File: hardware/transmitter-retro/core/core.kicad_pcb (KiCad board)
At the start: 2 copper layers, 100 x 90 mm, 64 parts, among them J1 Input, J2 Output, J3 Power, J4 Expansion, U1 556, U10 74LS163, U11 TLC7524CN, U12 74LS245, U13 74LS153, U14 74LS04, U15 74LS74, U16 74LS74, U18 74LS32, U19 74LS08, U2 74LS163, U21 LM339, U6 74LS153, U7 74LS273, U8 74LS165, U9 74LS163, Y1 4Mz

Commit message: Update part numbers Swap out input connector footprint Placement tweaks
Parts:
- removed C19: .01uF, Capacitor_THT:C_Rect_L4.6mm_W2.0mm_P2.50mm_MKS02_FKP02
- removed C29, C30: CP1, Capacitor_THT:CP_Radial_D4.0mm_P1.50mm
- removed C35: .001uF, Capacitor_THT:C_Rect_L4.6mm_W2.0mm_P2.50mm_MKS02_FKP02
- removed U18: 74LS32, Package_DIP:DIP-14_W7.62mm
- removed U19: 74LS08, Package_DIP:DIP-14_W7.62mm
- removed U21: LM339, Package_DIP:DIP-14_W7.62mm
- removed Y1: 4Mz, Crystal:Crystal_HC49-U_Vertical
- added C22: CP1, Capacitor_THT:CP_Radial_D4.0mm_P1.50mm, F.Cu at (170.4, 61.3)
- added R12: 10k, Resistor_THT:R_Axial_DIN0207_L6.3mm_D2.5mm_P10.16mm_Horizontal, F.Cu at (166.1, 136.5)
- added R13: 10k, Resistor_THT:R_Axial_DIN0207_L6.3mm_D2.5mm_P10.16mm_Horizontal, F.Cu at (143.4, 136.5)
- added R14: 10k, Resistor_THT:R_Axial_DIN0207_L6.3mm_D2.5mm_P10.16mm_Horizontal, F.Cu at (129.3, 92.6)
- added R15: 10k, Resistor_THT:R_Axial_DIN0207_L6.3mm_D2.5mm_P10.16mm_Horizontal, F.Cu at (177.5, 114.0)
- added R3: 1M, Resistor_THT:R_Axial_DIN0207_L6.3mm_D2.5mm_P10.16mm_Horizontal, F.Cu at (102.9, 52.3)
- added U17: ULN2003A, Package_DIP:DIP-16_W7.62mm, F.Cu at (103.9, 120.4)
- added U3: 74LS163, Package_DIP:DIP-16_W7.62mm, F.Cu at (133.6, 59.7)
- added U4: 74LS74, Package_DIP:DIP-14_W7.62mm, F.Cu at (144.7, 70.6)
- added U5: 74LS74, Package_DIP:DIP-14_W7.62mm, F.Cu at (156.1, 70.4)
- C21: value .01uF -> CP1; footprint Capacitor_THT:C_Rect_L4.6mm_W2.0mm_P2.50mm_MKS02_FKP02 -> Capacitor_THT:CP_Radial_D4.0mm_P1.50mm
- J1: footprint Connector_PinHeader_2.54mm:PinHeader_2x08_P2.54mm_Vertical -> Connector_IDC:IDC-Header_2x08_P2.54mm_Horizontal
- R10, R9: value 100k -> 10k
- R6, R7: value 2.2k -> 10k
- U10: value 74LS163 -> 74LS165
- U11: value TLC7524CN -> 74LS151
- U12: value 74LS245 -> 74LS163; footprint Package_DIP:DIP-20_W7.62mm -> Package_DIP:DIP-16_W7.62mm
- U13: value 74LS153 -> 74LS163
- U14: value 74LS04 -> 74LS373; footprint Package_DIP:DIP-14_W7.62mm -> Package_DIP:DIP-20_W7.62mm
- U15: value 74LS74 -> TLC7524CN; footprint Package_DIP:DIP-14_W7.62mm -> Package_DIP:DIP-20_W7.62mm
- U16: value 74LS74 -> LM339; footprint Package_DIP:DIP-14_W7.62mm -> Package_DIP:DIP-16_W7.62mm
- U2: value 74LS163 -> 74LS151
- U6: value 74LS153 -> 74LS08; footprint Package_DIP:DIP-16_W7.62mm -> Package_DIP:DIP-14_W7.62mm
- U7: value 74LS273 -> 74LS32; footprint Package_DIP:DIP-20_W7.62mm -> Package_DIP:DIP-14_W7.62mm
- U8: value 74LS165 -> 74LS04; footprint Package_DIP:DIP-16_W7.62mm -> Package_DIP:DIP-14_W7.62mm
- U9: value 74LS163 -> 74LS02; footprint Package_DIP:DIP-16_W7.62mm -> Package_DIP:DIP-14_W7.62mm
- moved R9 86.4 mm to (144.7, 53.2), turned to 270 degrees
- moved C5 83.6 mm to (166.6, 70.1)
- moved R8 83.3 mm to (152.0, 53.2), turned to 270 degrees
- moved R10 76.4 mm to (167.5, 75.9), turned to 270 degrees
- moved U9 68.8 mm to (156.1, 117.6)
- moved C21 68.8 mm to (170.4, 56.0), turned to 0 degrees
- moved C9 68.7 mm to (163.4, 114.4)
- moved J3 67.6 mm to (164.0, 59.9), turned to 180 degrees
- moved U10 66.4 mm to (166.5, 115.1)
- moved C10 66.2 mm to (173.9, 111.9)
- moved U12 63.9 mm to (145.8, 115.2)
- moved C12 63.5 mm to (153.2, 111.8)
- moved D1 60.2 mm to (156.2, 64.9), turned to 0 degrees
- moved C33 59.7 mm to (117.9, 62.0)
- moved R7 58.3 mm to (148.3, 53.2), turned to 270 degrees
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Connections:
- A1 pad 1: /SAMPLE_LATCH -> /~SAMPLE_OVERRIDE
- A1 pad 10: /SHIFT_TRANSMIT -> /~SHIFT_ENABLE
- A1 pad 11: /CLK_RX -> /SHIFT_TRANSMIT
- A1 pad 12: /monitor/DATA_RX_IN -> /DATA_RX
- A1 pad 13: /CLK_FAST -> /CLK_RX
- A1 pad 14: /CLK_SLOW -> /CLK_FAST
- A1 pad 15: /~SAMPLE_ASSERT -> /CLK_SLOW
- A1 pad 5: /~SAMPLE_RESET -> /SAMPLE_LATCH
- A1 pad 6: /SAMPLE_SEL0 -> /~SAMPLE_RESET
- A1 pad 7: /SAMPLE_SEL1 -> /SAMPLE_SEL0
- A1 pad 8: /~SHIFT_LOAD -> /SAMPLE_SEL1
- A1 pad 9: /SHIFT_DISABLE -> /~SHIFT_LOAD
- J1 pad 3: /monitor/DATA_RX_IN -> /shift/~CLK_OUT
- J1 pad 5: /CLK_RX -> /shift/~DATA_OUT
- J2 pad 3: /monitor/DATA_RX_IN -> /DATA_RX
- J4 pad 10: /~SAMPLE_RESET -> /SAMPLE_LATCH
- J4 pad 12: /SAMPLE_SEL0 -> /~SAMPLE_RESET
- J4 pad 14: /SAMPLE_SEL1 -> /SAMPLE_SEL0
- J4 pad 16: /~SHIFT_LOAD -> /SAMPLE_SEL1
- J4 pad 18: /SHIFT_DISABLE -> /~SHIFT_LOAD
- J4 pad 20: /SHIFT_TRANSMIT -> /~SHIFT_ENABLE
- J4 pad 21: /CLK_TX -> /~BUS_ACK
- J4 pad 22: /DATA_FIXED -> /SHIFT_TRANSMIT
- J4 pad 23: /CLK_RX -> /~BUS_REQ
- J4 pad 24: /~FRAME_RESET -> Net-(J4-Pad24)
- J4 pad 25: /CLK_FAST -> /SAMPLE_REF
- J4 pad 26: Net-(J4-Pad26) -> /~FRAME_RESET
- J4 pad 27: /CLK_SLOW -> /CLK_EXT
- J4 pad 28: Net-(J4-Pad28) -> /DATA_RX
- J4 pad 29: Net-(J4-Pad29) -> /CLK_TX
- J4 pad 30: Net-(J4-Pad30) -> /DATA_FIXED
- J4 pad 31: Net-(J4-Pad31) -> /CLK_RX
- J4 pad 32: Net-(J4-Pad32) -> /DATA_SHIFT
- J4 pad 33: Net-(J4-Pad33) -> /CLK_FAST
- J4 pad 34: Net-(J4-Pad34) -> GND
- J4 pad 35: Net-(J4-Pad35) -> /CLK_SLOW
- J4 pad 36: Net-(J4-Pad36) -> GND
- J4 pad 37: GND -> Net-(J4-Pad37)
- J4 pad 39: GND -> /~CLK_EXT_SEL
- J4 pad 6: /~SAMPLE_ASSERT -> /SAMPLE_COUNT
- J4 pad 8: /SAMPLE_LATCH -> /~SAMPLE_OVERRIDE
- R10 pad 1: /clock/~CLK_SLOW_IN -> +5V
- R10 pad 2: GND -> /shift/~CLK_STEP_IN
- R11 pad 2: /shift/~CLK_STEP_IN -> /clock/~CLK_STEP_INA
- R6 pad 1: Net-(R6-Pad1) -> +5V
- R6 pad 2: Net-(R6-Pad2) -> /CLK_EXT
- R7 pad 1: Net-(R7-Pad1) -> +5V
- R7 pad 2: Net-(R6-Pad1) -> /clock/~CLK_SLOW_IN
- R8 pad 1: /clock/~CLK_STEP_INA -> +5V
- R8 pad 2: GND -> /clock/~CLK_FAST_IN
- R9 pad 1: /clock/~CLK_FAST_IN -> +5V
- R9 pad 2: GND -> /~CLK_EXT_SEL
- U1 pad 5: Net-(U1-Pad5) -> /clock/CLK_SLOW
- U1 pad 9: Net-(U1-Pad9) -> /clock/CLK_FAST
- U10 pad 1: /~SAMPLE_RESET -> /~SHIFT_LOAD
- U10 pad 10: Net-(U10-Pad10) -> GND
- U10 pad 11: /sample/DO7 -> /shift/D0
- U10 pad 12: /sample/DO6 -> /shift/D1
- U10 pad 13: /sample/DO5 -> /shift/D2
- U10 pad 14: /sample/DO4 -> /shift/D3
- U10 pad 15: Net-(U10-Pad15) -> /~SHIFT_ENABLE
- U10 pad 2: /clock/CLK_SAMPLE_OUT -> /CLK_TX
- U10 pad 3: GND -> /shift/D4
- U10 pad 4: GND -> /shift/D5
- U10 pad 5: GND -> /shift/D6
- U10 pad 6: GND -> /shift/D7
- U10 pad 7: +5V -> Net-(U10-Pad7)
- U10 pad 9: +5V -> /DATA_SHIFT
- U11 pad 1: +5V -> Net-(U11-Pad1)
- U11 pad 10: /sample/DO1 -> Net-(U11-Pad10)
- U11 pad 11: /sample/DO0 -> Net-(U11-Pad11)
- U11 pad 12: GND -> Net-(U11-Pad12)
- U11 pad 13: /clock/CLK_SAMPLE_OUT -> Net-(U11-Pad13)
- U11 pad 14: +5V -> Net-(U11-Pad14)
- U11 pad 15: Net-(U11-Pad15) -> /SAMPLE_COUNT
- U11 pad 16: Net-(U11-Pad16) -> +5V
- U11 pad 2: GND -> Net-(U11-Pad2)
- U11 pad 3: GND -> Net-(U11-Pad3)
- U11 pad 4: /sample/DO7 -> Net-(U11-Pad4)
- U11 pad 5: /sample/DO6 -> Net-(U11-Pad5)
- U11 pad 6: /sample/DO5 -> Net-(U11-Pad6)
- U11 pad 7: /sample/DO4 -> GND
- U11 pad 8: /sample/DO3 -> GND
- U11 pad 9: /sample/DO2 -> /~SAMPLE_OVERRIDE
- U12 pad 1: +5V -> /~SAMPLE_RESET
- U12 pad 10: GND -> Net-(U12-Pad10)
- U12 pad 11: /sample/D7 -> /sample/DO3
- U12 pad 12: /sample/D6 -> /sample/DO2
- U12 pad 13: /sample/D5 -> /sample/D01
- U12 pad 14: /sample/D4 -> /sample/DO0
- U12 pad 15: /sample/D3 -> Net-(U12-Pad15)
- U12 pad 16: /sample/D2 -> +5V
- U12 pad 2: Net-(U12-Pad2) -> /clock/CLK_SAMPLE_OUT
- U12 pad 3: Net-(U12-Pad3) -> GND
- U12 pad 4: Net-(U12-Pad4) -> GND
- U12 pad 5: Net-(U12-Pad5) -> GND
- U12 pad 6: Net-(U12-Pad6) -> GND
- U12 pad 7: Net-(U12-Pad7) -> Net-(U11-Pad5)
- U12 pad 8: Net-(U12-Pad8) -> GND
- U12 pad 9: Net-(U12-Pad9) -> +5V
- U13 pad 1: GND -> /~SAMPLE_RESET
- U13 pad 10: GND -> Net-(U12-Pad15)
- U13 pad 11: GND -> /sample/DO7
- U13 pad 12: GND -> /sample/DO6
- U13 pad 13: GND -> /sample/DO5
- U13 pad 14: /CLK_SLOW -> /sample/DO4
- U13 pad 15: GND -> Net-(U13-Pad15)
- U13 pad 2: /CLK_FAST -> /clock/CLK_SAMPLE_OUT
- U13 pad 3: Net-(U13-Pad3) -> GND
- U13 pad 4: Net-(U1-Pad5) -> GND
- U13 pad 5: Net-(U1-Pad9) -> GND
- U13 pad 6: Net-(R7-Pad1) -> GND
- U13 pad 7: /clock/CLK_SAMPLE_OUT -> +5V
- U13 pad 9: Net-(U13-Pad9) -> +5V
- U14 pad 1: Net-(R6-Pad2) -> Net-(U14-Pad1)
- U14 pad 10: Net-(U14-Pad10) -> GND
- U14 pad 11: Net-(U10-Pad15) -> /SAMPLE_LATCH
- U14 pad 12: Net-(U14-Pad12) -> /sample/D4
- U14 pad 13: Net-(U14-Pad13) -> /sample/DO4
- U14 pad 14: +5V -> /sample/DO5
- U14 pad 2: Net-(R6-Pad1) -> /sample/D0
- U14 pad 3: Net-(R6-Pad1) -> /sample/DO0
- U14 pad 4: Net-(R7-Pad1) -> /sample/D01
- U14 pad 5: Net-(U14-Pad5) -> /sample/D1
- U14 pad 6: Net-(U14-Pad6) -> /sample/D2
- U14 pad 7: GND -> /sample/DO2
- U14 pad 8: /CLK_RX -> /sample/DO3
- U14 pad 9: /CLK_TX -> /sample/D3
- U15 pad 10: Net-(U14-Pad12) -> /sample/DO1
- U15 pad 11: Net-(U13-Pad3) -> /sample/DO0
- U15 pad 12: /CLK_TX -> GND
- U15 pad 13: Net-(U15-Pad13) -> /clock/CLK_SAMPLE_OUT
- U15 pad 2: Net-(U15-Pad2) -> GND
- U15 pad 3: Net-(U1-Pad9) -> GND
- U15 pad 4: +5V -> /sample/DO7
- U15 pad 5: Net-(U15-Pad5) -> /sample/DO6
- U15 pad 6: Net-(U15-Pad6) -> /sample/DO5
- U15 pad 7: GND -> /sample/DO4
- U15 pad 8: Net-(U15-Pad8) -> /sample/DO3
- U15 pad 9: Net-(U15-Pad9) -> /sample/DO2
- U16 pad 1: Net-(U16-Pad1) -> Net-(U11-Pad3)
- U16 pad 10: Net-(U16-Pad10) -> /SAMPLE_REF
- U16 pad 11: /CLK_TX -> /sample/DIM_2_IN
- U16 pad 12: /clock/~CLK_FAST_IN -> GND
- U16 pad 13: Net-(U16-Pad10) -> Net-(U11-Pad2)
- U16 pad 14: +5V -> Net-(U11-Pad1)
- U16 pad 2: /clock/~CLK_SLOW_IN -> Net-(U11-Pad4)
- U16 pad 3: /CLK_TX -> +5V
- U16 pad 4: Net-(U16-Pad1) -> /SAMPLE_REF
- U16 pad 5: /CLK_SLOW -> /sample/DIM_4_IN
- U16 pad 6: Net-(U16-Pad6) -> /SAMPLE_REF
- U16 pad 7: GND -> /sample/DIM_3_IN
- U16 pad 8: Net-(U16-Pad8) -> /SAMPLE_REF
- U16 pad 9: /CLK_FAST -> /sample/DIM_1_IN
- U2 pad 1: +5V -> /clock/CLK_STEP
- U2 pad 10: +5V -> /CLK_FAST
- U2 pad 11: /CLK_TX -> /CLK_SLOW
- U2 pad 2: /clock/CLK_SAMPLE_OUT -> /clock/CLK_SLOW
- U2 pad 3: GND -> /clock/CLK_FAST
- U2 pad 4: GND -> /CLK_EXT
- U2 pad 5: GND -> /clock/CLK_SAMPLE_OUT
- U2 pad 6: GND -> Net-(U2-Pad6)
- U2 pad 7: +5V -> GND
- U2 pad 9: +5V -> GND
- U6 pad 1: GND -> /DATA_SHIFT
- U6 pad 10: GND -> Net-(U6-Pad10)
- U6 pad 11: GND -> Net-(U5-Pad2)
- U6 pad 12: GND -> /shift/~CLK_STEP_IN
- U6 pad 13: GND -> /clock/~CLK_STEP_INA
- U6 pad 14: /SAMPLE_SEL0 -> +5V
- U6 pad 2: /SAMPLE_SEL1 -> /SHIFT_TRANSMIT
- U6 pad 3: Net-(U21-Pad14) -> Net-(U6-Pad3)
- U6 pad 4: Net-(U21-Pad13) -> /clock/CLK_FAST
- U6 pad 5: Net-(U21-Pad1) -> Net-(U6-Pad5)
- U6 pad 6: Net-(U21-Pad2) -> /clock/CLK_STEP
- U6 pad 7: Net-(U6-Pad7) -> GND
- U6 pad 8: GND -> Net-(U6-Pad8)
- U6 pad 9: Net-(U6-Pad9) -> Net-(U5-Pad13)
- U7 pad 1: +5V -> Net-(U6-Pad3)
- U7 pad 10: GND -> Net-(U5-Pad2)
- U7 pad 11: /SAMPLE_LATCH -> Net-(U6-Pad5)
- U7 pad 12: Net-(U12-Pad6) -> /CLK_TX
- U7 pad 13: /sample/DO4 -> Net-(U5-Pad8)
- U7 pad 14: /sample/DO5 -> +5V
- U7 pad 2: Net-(U12-Pad2) -> /DATA_FIXED
- U7 pad 3: /sample/DO0 -> /DATA_RX
- U7 pad 4: /sample/D01 -> +5V
- U7 pad 5: Net-(U12-Pad3) -> +5V
- U7 pad 6: Net-(U12-Pad4) -> Net-(U7-Pad6)
- U7 pad 7: /sample/DO2 -> GND
- U7 pad 8: /sample/DO3 -> Net-(U5-Pad13)
- U7 pad 9: Net-(U12-Pad5) -> Net-(U5-Pad6)
- U8 pad 1: /~SHIFT_LOAD -> /~BUS_REQ
- U8 pad 10: GND -> Net-(U8-Pad10)
- U8 pad 11: /shift/D0 -> +5V
- U8 pad 12: /shift/D1 -> Net-(U5-Pad10)
- U8 pad 13: /shift/D2 -> Net-(U6-Pad8)
- U8 pad 14: /shift/D3 -> +5V
- U8 pad 2: /CLK_TX -> Net-(U14-Pad1)
- U8 pad 3: /shift/D4 -> Net-(U14-Pad1)
- U8 pad 4: /shift/D5 -> /~BUS_ACK
- U8 pad 5: /shift/D6 -> Net-(U6-Pad5)
- U8 pad 6: /shift/D7 -> Net-(U6-Pad10)
- U8 pad 7: Net-(U8-Pad7) -> GND
- U8 pad 8: GND -> /CLK_RX
- U8 pad 9: Net-(U19-Pad1) -> /CLK_TX
- U9 pad 1: /~SAMPLE_RESET -> Net-(U11-Pad11)
- U9 pad 10: Net-(U14-Pad10) -> Net-(U12-Pad10)
- U9 pad 11: /sample/DO3 -> +5V
- U9 pad 12: /sample/DO2 -> +5V
- U9 pad 13: /sample/D01 -> Net-(U9-Pad13)
- U9 pad 14: /sample/DO0 -> +5V
- U9 pad 2: /clock/CLK_SAMPLE_OUT -> /~SAMPLE_OVERRIDE
- U9 pad 3: GND -> /SAMPLE_SEL0
- U9 pad 4: GND -> Net-(U11-Pad10)
- U9 pad 5: GND -> /~SAMPLE_OVERRIDE
- U9 pad 6: GND -> /SAMPLE_SEL1
- U9 pad 7: Net-(U6-Pad7) -> GND
- U9 pad 8: GND -> Net-(U13-Pad15)
- U9 pad 9: +5V -> Net-(U13-Pad15)
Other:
- board text added: "DMX-TX3"
- board text added: "DMX-TX3, Rev 1.2 Crazy Giraffe Software"
- board text added: "Power"
- board text removed: "DMX-CPCB, Rev 1.2 Crazy Giraffe Software"

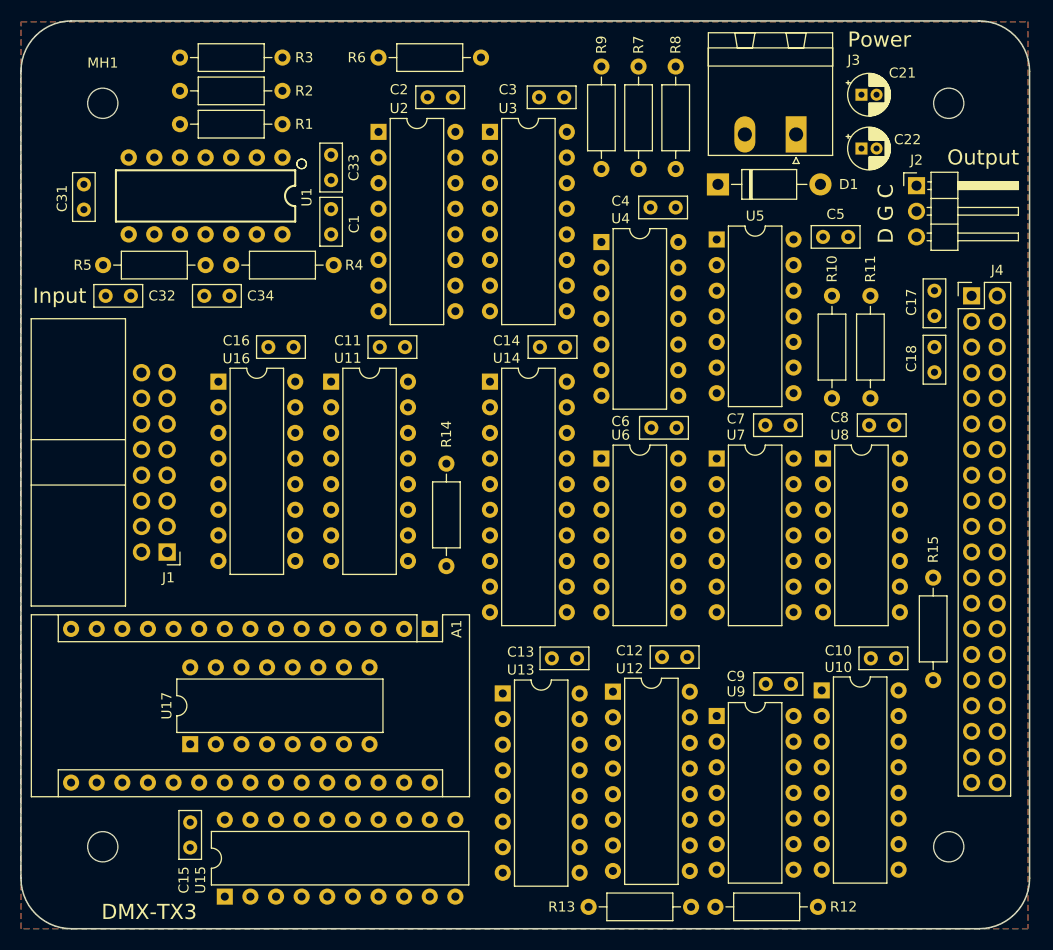
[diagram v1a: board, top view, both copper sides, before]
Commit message: Prototype and PCB layout for core Prototype and PCB layout for demo Prototype and PCB layout for control-eprom Move display design forward Refactor control-dmx to dmx Update expansion connector on all boards Add test suites Add tx-retro readme Cleanup
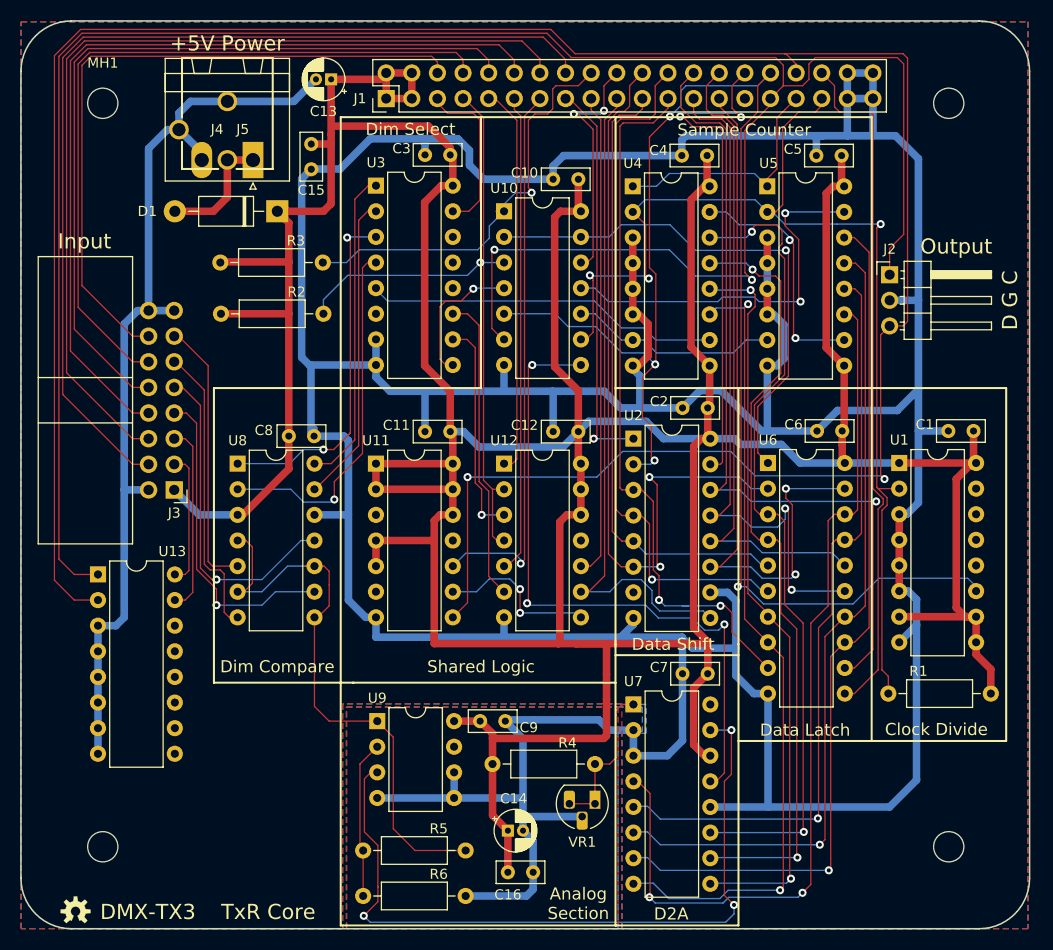
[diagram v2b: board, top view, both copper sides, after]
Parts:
- removed A1: Monitor, Module:Arduino_Nano
- removed C17, C18, C33, C34: .01uF, Capacitor_THT:C_Rect_L4.6mm_W2.0mm_P2.50mm_MKS02_FKP02
- removed C21, C22: CP1, Capacitor_THT:CP_Radial_D4.0mm_P1.50mm
- removed C31: 1uF, Capacitor_THT:C_Rect_L4.6mm_W2.0mm_P2.50mm_MKS02_FKP02
- removed C32: .001uF, Capacitor_THT:C_Rect_L4.6mm_W2.0mm_P2.50mm_MKS02_FKP02
- removed R10, R11, R12, R13, R14, R15, R7, R8, R9: 10k, Resistor_THT:R_Axial_DIN0207_L6.3mm_D2.5mm_P10.16mm_Horizontal
- removed U14: 74LS373, Package_DIP:DIP-20_W7.62mm
- removed U15: TLC7524CN, Package_DIP:DIP-20_W7.62mm
- removed U16: LM339, Package_DIP:DIP-16_W7.62mm
- removed U17: ULN2003A, Package_DIP:DIP-16_W7.62mm
- added ?: , footprints:OSHW-LOGO-S, F.Cu at (92.5, 137.0)
- added G***: LOGO, footprints:logo_cr_5x5, B.Cu at (105.7, 131.6)
- added J5: Power, Connectors:POWER_JACK_PTH_BREAD, F.Cu at (107.6, 48.8)
- added VR1: TL1431, Package_TO_SOT_THT:TO-92L_HandSolder, F.Cu at (144.0, 126.3)
- C13, C14: value .01uF -> 10uF; footprint Capacitor_THT:C_Rect_L4.6mm_W2.0mm_P2.50mm_MKS02_FKP02 -> Capacitor_THT:CP_Radial_D4.0mm_P1.50mm
- J1: value Input -> Expansion; footprint Connector_IDC:IDC-Header_2x08_P2.54mm_Horizontal -> Connector_PinHeader_2.54mm:PinHeader_2x20_P2.54mm_Vertical
- J3: value Power -> Input; footprint Connector_Phoenix_MSTB:PhoenixContact_MSTBA_2,5_2-G-5,08_1x02_P5.08mm_Horizontal -> Connector_IDC:IDC-Header_2x08_P2.54mm_Horizontal
- J4: value Expansion -> Power; footprint Connector_PinHeader_2.54mm:PinHeader_2x20_P2.54mm_Vertical -> Connector_Phoenix_MSTB:PhoenixContact_MSTBA_2,5_2-G-5,08_1x02_P5.08mm_Horizontal
- R1: value 2.2k -> 10k
- R2: value 100 -> 10k
- R3: value 1M -> 10k
- R4: value 1k -> 1.6k
- R5: value 3.3k -> 10k
- U1: value 556 -> 74LS163; footprint Silicon-Standard:DIP14 -> Package_DIP:DIP-16_W7.62mm
- U10: value 74LS165 -> 74LS04; footprint Package_DIP:DIP-16_W7.62mm -> Package_DIP:DIP-14_W7.62mm
- U11: value 74LS151 -> 74LS32; footprint Package_DIP:DIP-16_W7.62mm -> Package_DIP:DIP-14_W7.62mm
- U12: value 74LS163 -> 74LS08; footprint Package_DIP:DIP-16_W7.62mm -> Package_DIP:DIP-14_W7.62mm
- U13: value 74LS163 -> ULN2003A
- U2: value 74LS151 -> 74LS165
- U3: value 74LS163 -> 74LS151
- U4, U5: value 74LS74 -> 74LS163; footprint Package_DIP:DIP-14_W7.62mm -> Package_DIP:DIP-16_W7.62mm
- U6: value 74LS08 -> 74LS373; footprint Package_DIP:DIP-14_W7.62mm -> Package_DIP:DIP-20_W7.62mm
- U7: value 74LS32 -> TLC7524CN; footprint Package_DIP:DIP-14_W7.62mm -> Package_DIP:DIP-16_W7.62mm
- U8: value 74LS04 -> LM339
- U9: value 74LS02 -> TLV2772CP; footprint Package_DIP:DIP-14_W7.62mm -> Package_DIP:DIP-8_W7.62mm
- moved R1 90.1 mm to (173.1, 115.4)
- moved R6 83.1 mm to (131.2, 135.4)
- moved U1 73.7 mm to (174.2, 92.5), turned to 0 degrees
- moved J4 72.5 mm to (110.1, 62.5), turned to 180 degrees
- moved J3 71.0 mm to (102.3, 95.2)
- moved C15 68.3 mm to (115.9, 60.9)
- moved C1 66.6 mm to (181.5, 89.3), turned to 180 degrees
- moved C13 62.4 mm to (117.9, 54.5)
- moved R5 60.1 mm to (121.0, 130.9), turned to 0 degrees
- moved U8 58.0 mm to (108.6, 92.6)
- moved C8 57.5 mm to (113.7, 89.9)
- moved C16 57.2 mm to (135.4, 133.1)
- moved C10 57.0 mm to (142.4, 64.4)
- moved U10 57.0 mm to (135.0, 67.6)
- moved R4 55.8 mm to (144.0, 122.4)
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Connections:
- J1 pad 10: /clock/~CLK_STEP_INA -> /~CLK_STEP
- J1 pad 11: /sample/DIM_3_IN -> /SAMPLE_SEL0
- J1 pad 12: /clock/~CLK_SLOW_IN -> /SPD_LO
- J1 pad 13: /sample/DIM_4_IN -> /DATA_FIXED
- J1 pad 14: /clock/~CLK_FAST_IN -> /SPD_MID
- J1 pad 15: GND -> /~SHIFT_LOAD
- J1 pad 16: GND -> /SPD_HI
- J1 pad 2: GND -> +5V
- J1 pad 3: /shift/~CLK_OUT -> +5V
- J1 pad 4: Net-(J1-Pad4) -> +5V
- J1 pad 5: /shift/~DATA_OUT -> /SAMPLE_COUNT
- J1 pad 6: /clock/SPD_WIPER -> /~CLK_FST
- J1 pad 7: /sample/DIM_1_IN -> /~SAMPLE_OVERRIDE
- J1 pad 8: /clock/SPD_LO -> /~CLK_SLO
- J1 pad 9: /sample/DIM_2_IN -> /SAMPLE_SEL1
- J3 pad 1: Net-(D1-Pad2) -> +5V
- J4 pad 1: +5V -> Net-(D1-Pad2)
- J4 pad 2: +5V -> GND
- R1 pad 1: +5V -> /CLK_SAMPLE
- R1 pad 2: Net-(R1-Pad2) -> +5V
- R2 pad 1: Net-(R1-Pad2) -> +5V
- R2 pad 2: /clock/SPD_WIPER -> /~SAMPLE_OVERRIDE
- R3 pad 1: /clock/SPD_WIPER -> +5V
- R3 pad 2: /clock/SPD_LO -> /~BUS_REQ
- R4 pad 1: +5V -> Net-(R4-Pad1)
- R4 pad 2: Net-(R4-Pad2) -> +5V
- R5 pad 1: Net-(R4-Pad2) -> Net-(R5-Pad1)
- R5 pad 2: Net-(C32-Pad1) -> Net-(R5-Pad2)
- R6 pad 1: +5V -> GND
- R6 pad 2: /CLK_EXT -> Net-(R5-Pad1)
- U1 pad 1: Net-(R1-Pad2) -> +5V
- U1 pad 11: Net-(C34-Pad1) -> /CLK_TX
- U1 pad 12: Net-(C32-Pad1) -> Net-(U1-Pad12)
- U1 pad 13: Net-(R4-Pad2) -> Net-(U1-Pad13)
- U1 pad 14: +5V -> Net-(U1-Pad14)
- U1 pad 2: /clock/SPD_LO -> /CLK_SAMPLE
- U1 pad 3: Net-(C33-Pad1) -> GND
- U1 pad 4: +5V -> GND
- U1 pad 5: /clock/CLK_SLOW -> GND
- U1 pad 6: /clock/SPD_LO -> GND
- U1 pad 7: GND -> +5V
- U1 pad 8: Net-(C32-Pad1) -> GND
- U1 pad 9: /clock/CLK_FAST -> +5V
- U10 pad 1: /~SHIFT_LOAD -> /~BUS_REQ
- U10 pad 10: GND -> Net-(U10-Pad10)
- U10 pad 11: /shift/D0 -> Net-(U10-Pad11)
- U10 pad 12: /shift/D1 -> /~BUS_ACK
- U10 pad 13: /shift/D2 -> Net-(U10-Pad13)
- U10 pad 14: /shift/D3 -> +5V
- U10 pad 2: /CLK_TX -> Net-(U10-Pad13)
- U10 pad 3: /shift/D4 -> /~SAMPLE_OVERRIDE
- U10 pad 4: /shift/D5 -> Net-(U10-Pad4)
- U10 pad 5: /shift/D6 -> /CLK_TX
- U10 pad 6: /shift/D7 -> /CLK_RX
- U10 pad 7: Net-(U10-Pad7) -> GND
- U10 pad 8: GND -> Net-(U10-Pad8)
- U10 pad 9: /DATA_SHIFT -> /CLK_SAMPLE
- U11 pad 1: Net-(U11-Pad1) -> +5V
- U11 pad 10: Net-(U11-Pad10) -> /DATA_FIXED
- U11 pad 12: Net-(U11-Pad12) -> +5V
- U11 pad 13: Net-(U11-Pad13) -> +5V
- U11 pad 14: Net-(U11-Pad14) -> +5V
- U11 pad 2: Net-(U11-Pad2) -> +5V
- U11 pad 4: Net-(U11-Pad4) -> +5V
- U11 pad 5: Net-(U11-Pad5) -> +5V
- U11 pad 8: GND -> /DATA_RX
- U11 pad 9: /~SAMPLE_OVERRIDE -> Net-(U11-Pad9)
- U12 pad 1: /~SAMPLE_RESET -> /SAMPLE_SEL1
- U12 pad 10: Net-(U12-Pad10) -> /SHIFT_TRANSMIT
- U12 pad 11: /sample/DO3 -> Net-(U12-Pad11)
- U12 pad 12: /sample/DO2 -> +5V
- U12 pad 13: /sample/D01 -> +5V
- U12 pad 14: /sample/DO0 -> +5V
- U12 pad 2: /clock/CLK_SAMPLE_OUT -> /~SAMPLE_OVERRIDE
- U12 pad 3: GND -> Net-(U12-Pad3)
- U12 pad 4: GND -> /~SAMPLE_OVERRIDE
- U12 pad 5: GND -> /SAMPLE_SEL0
- U12 pad 6: GND -> Net-(U12-Pad6)
- U12 pad 7: Net-(U11-Pad5) -> GND
- U12 pad 8: GND -> Net-(U11-Pad9)
- U12 pad 9: +5V -> /DATA_SHIFT
- U13 pad 1: /~SAMPLE_RESET -> /CLK_RX
- U13 pad 10: Net-(U12-Pad15) -> Net-(U13-Pad10)
- U13 pad 11: /sample/DO7 -> Net-(U13-Pad11)
- U13 pad 12: /sample/DO6 -> Net-(U13-Pad12)
- U13 pad 13: /sample/DO5 -> Net-(U13-Pad13)
- U13 pad 14: /sample/DO4 -> Net-(U13-Pad14)
- U13 pad 15: Net-(U13-Pad15) -> /~DATA
- U13 pad 16: +5V -> /~CLOCK
- U13 pad 2: /clock/CLK_SAMPLE_OUT -> /DATA_RX
- U13 pad 7: +5V -> GND
- U13 pad 9: +5V -> Net-(U13-Pad9)
- U2 pad 1: /clock/CLK_STEP -> /~SHIFT_LOAD
- U2 pad 10: /CLK_FAST -> GND
- U2 pad 11: /CLK_SLOW -> /D7
- U2 pad 12: Net-(U2-Pad12) -> /D6
- U2 pad 13: Net-(U2-Pad13) -> /D5
- U2 pad 14: Net-(U2-Pad14) -> /D4
- U2 pad 15: Net-(U2-Pad15) -> /~SHIFT_ENABLE
- U2 pad 2: /clock/CLK_SLOW -> /CLK_TX
- U2 pad 3: /clock/CLK_FAST -> /D3
- U2 pad 4: /CLK_EXT -> /D2
- U2 pad 5: /clock/CLK_SAMPLE_OUT -> /D1
- U2 pad 6: Net-(U2-Pad6) -> /D0
- U2 pad 7: GND -> Net-(U2-Pad7)
- U2 pad 9: GND -> /DATA_SHIFT
- U3 pad 1: +5V -> Net-(U3-Pad1)
- U3 pad 10: +5V -> Net-(U12-Pad3)
- U3 pad 11: /CLK_TX -> Net-(U12-Pad6)
- U3 pad 15: Net-(U3-Pad15) -> /SAMPLE_COUNT
- U3 pad 2: /clock/CLK_SAMPLE_OUT -> Net-(U3-Pad2)
- U3 pad 3: GND -> Net-(U3-Pad3)
- U3 pad 4: GND -> Net-(U3-Pad4)
- U3 pad 5: GND -> Net-(U3-Pad5)
- U3 pad 6: GND -> Net-(U3-Pad6)
- U3 pad 7: +5V -> GND
- U3 pad 9: +5V -> Net-(U10-Pad4)
- U4 pad 1: /~CLK_EXT_SEL -> /~SAMPLE_RESET
- U4 pad 10: +5V -> Net-(U3-Pad5)
- U4 pad 11: /clock/CLK_FAST -> /sample/DO3
- U4 pad 12: /clock/~CLK_FAST_IN -> /sample/DO2
- U4 pad 13: /~CLK_EXT_SEL -> /sample/DO1
- U4 pad 14: +5V -> /sample/DO0
- U4 pad 2: /clock/~CLK_SLOW_IN -> /CLK_SAMPLE
- U4 pad 3: /clock/CLK_FAST -> GND
- U4 pad 4: +5V -> GND
- U4 pad 5: /CLK_SLOW -> GND
- U4 pad 6: Net-(U4-Pad6) -> GND
- U4 pad 7: GND -> Net-(U10-Pad10)
- U4 pad 8: Net-(U4-Pad8) -> GND
- U4 pad 9: /CLK_FAST -> +5V
- U5 pad 1: +5V -> /~SAMPLE_RESET
- U5 pad 10: Net-(U5-Pad10) -> Net-(U4-Pad15)
- U5 pad 11: /clock/CLK_STEP -> /sample/DO7
- U5 pad 12: /CLK_TX -> /sample/DO6
- U5 pad 13: Net-(U5-Pad13) -> /sample/DO5
- U5 pad 14: +5V -> /sample/DO4
- U5 pad 2: Net-(U5-Pad2) -> /CLK_SAMPLE
- U5 pad 3: Net-(U5-Pad3) -> GND
- U5 pad 4: +5V -> GND
- U5 pad 5: Net-(U5-Pad5) -> GND
- U5 pad 6: Net-(U5-Pad6) -> GND
- U5 pad 7: GND -> Net-(U10-Pad10)
- U5 pad 8: Net-(U5-Pad8) -> GND
- U5 pad 9: Net-(U5-Pad9) -> +5V
- U6 pad 1: /DATA_SHIFT -> Net-(U10-Pad13)
- U6 pad 10: Net-(U6-Pad10) -> GND
- U6 pad 11: Net-(U5-Pad2) -> /SAMPLE_LATCH
- U6 pad 12: /shift/~CLK_STEP_IN -> /D4
- U6 pad 13: /clock/~CLK_STEP_INA -> /sample/DO4
- U6 pad 14: +5V -> /sample/DO5
- U6 pad 2: /SHIFT_TRANSMIT -> /D0
- U6 pad 3: Net-(U6-Pad3) -> /sample/DO0
- U6 pad 4: /clock/CLK_FAST -> /sample/DO1
- U6 pad 5: Net-(U6-Pad5) -> /D1
- U6 pad 6: /clock/CLK_STEP -> /D2
- U6 pad 7: GND -> /sample/DO2
- U6 pad 8: Net-(U6-Pad8) -> /sample/DO3
- U6 pad 9: Net-(U5-Pad13) -> /D3
- U7 pad 1: Net-(U6-Pad3) -> Net-(R4-Pad1)
- U7 pad 10: Net-(U5-Pad2) -> /sample/DO1
- U7 pad 11: Net-(U6-Pad5) -> /sample/DO0
- U7 pad 12: /CLK_TX -> GND
- U7 pad 13: Net-(U5-Pad8) -> Net-(U10-Pad8)
- U7 pad 2: /DATA_FIXED -> GND
- U7 pad 3: /DATA_RX -> GND
- U7 pad 4: +5V -> /sample/DO7
- U7 pad 5: +5V -> /sample/DO6
- U7 pad 6: Net-(U7-Pad6) -> /sample/DO5
- U7 pad 7: GND -> /sample/DO4
- U7 pad 8: Net-(U5-Pad13) -> /sample/DO3
- U7 pad 9: Net-(U5-Pad6) -> /sample/DO2
- U8 pad 1: /~BUS_REQ -> Net-(U3-Pad3)
- U8 pad 10: Net-(U8-Pad10) -> Net-(R5-Pad2)
- U8 pad 11: +5V -> /DIM2
- U8 pad 12: Net-(U5-Pad10) -> GND
- U8 pad 13: Net-(U6-Pad8) -> Net-(U3-Pad2)
- U8 pad 14: +5V -> Net-(U3-Pad1)
- U8 pad 2: Net-(U14-Pad1) -> Net-(U3-Pad4)
- U8 pad 3: Net-(U14-Pad1) -> +5V
- U8 pad 4: /~BUS_ACK -> Net-(R5-Pad2)
- U8 pad 5: Net-(U6-Pad5) -> /DIM4
- U8 pad 6: Net-(U6-Pad10) -> Net-(R5-Pad2)
- U8 pad 7: GND -> /DIM3
- U8 pad 8: /CLK_RX -> Net-(R5-Pad2)
- U8 pad 9: /CLK_TX -> /DIM1
- U9 pad 1: Net-(U11-Pad11) -> Net-(R5-Pad2)
- U9 pad 2: /~SAMPLE_OVERRIDE -> Net-(R5-Pad1)
- U9 pad 3: /SAMPLE_SEL0 -> Net-(U7-Pad15)
- U9 pad 4: Net-(U11-Pad10) -> GND
- U9 pad 5: /~SAMPLE_OVERRIDE -> GND
- U9 pad 6: /SAMPLE_SEL1 -> GND
- U9 pad 7: GND -> Net-(U9-Pad7)
- U9 pad 8: Net-(U13-Pad15) -> +5V
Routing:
- net GND: track 0.00 -> 600.2 mm
- net +5V: track 0.00 -> 492.7 mm
- net /DATA_RX: track 0.00 -> 249.0 mm, vias 0 -> 2
- net /CLK_RX: track 0.00 -> 223.6 mm, vias 0 -> 2
- net /CLK_TX: track 0.00 -> 146.6 mm, vias 0 -> 4
- net /CLK_SAMPLE: track 0.00 -> 111.5 mm, vias 0 -> 3
- net /SPD_HI: track 0.00 -> 97.7 mm
- net /SPD_MID: track 0.00 -> 91.7 mm
- net /sample/DO7: track 0.00 -> 90.0 mm, vias 0 -> 2
- net /sample/DO4: track 0.00 -> 86.5 mm, vias 0 -> 1
- net /SPD_LO: track 0.00 -> 86.3 mm
- net /sample/DO0: track 0.00 -> 81.7 mm, vias 0 -> 2
- net /D4: track 0.00 -> 81.7 mm, vias 0 -> 1
- net /sample/DO5: track 0.00 -> 80.6 mm, vias 0 -> 1
- net /~CLK_STEP: track 0.00 -> 80.3 mm
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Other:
- net class Default: trace_width 0.25 -> 0.127
- net class Gnd added: clearance 0.25, trace_width 0.75, via_dia 0.8, via_drill 0.4
- net class Power added: clearance 0.25, trace_width 0.75, via_dia 0.8, via_drill 0.4
- rule trace_min: 0.2 -> 0.127
- rule via_min_size: 0.4 -> 0.5
- board text added: "+5V Power"
- board text added: "Analog Section"
- board text added: "Clock Divide"
- board text added: "D2A"
- board text added: "DMX-TX3, Rev 1.0 Crazy Giraffe Software"
- board text added: "Data Latch"
- board text added: "Data Shift"
- board text added: "Dim Compare"
- board text added: "Dim Select"
- board text added: "Sample Counter"
- board text added: "Shared Logic"
- board text added: "TxR Core"
- board text removed: "DMX-TX3, Rev 1.2 Crazy Giraffe Software"
- board text removed: "Power"

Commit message: Rev 1.1 - Value labels - 74LS06 led driver
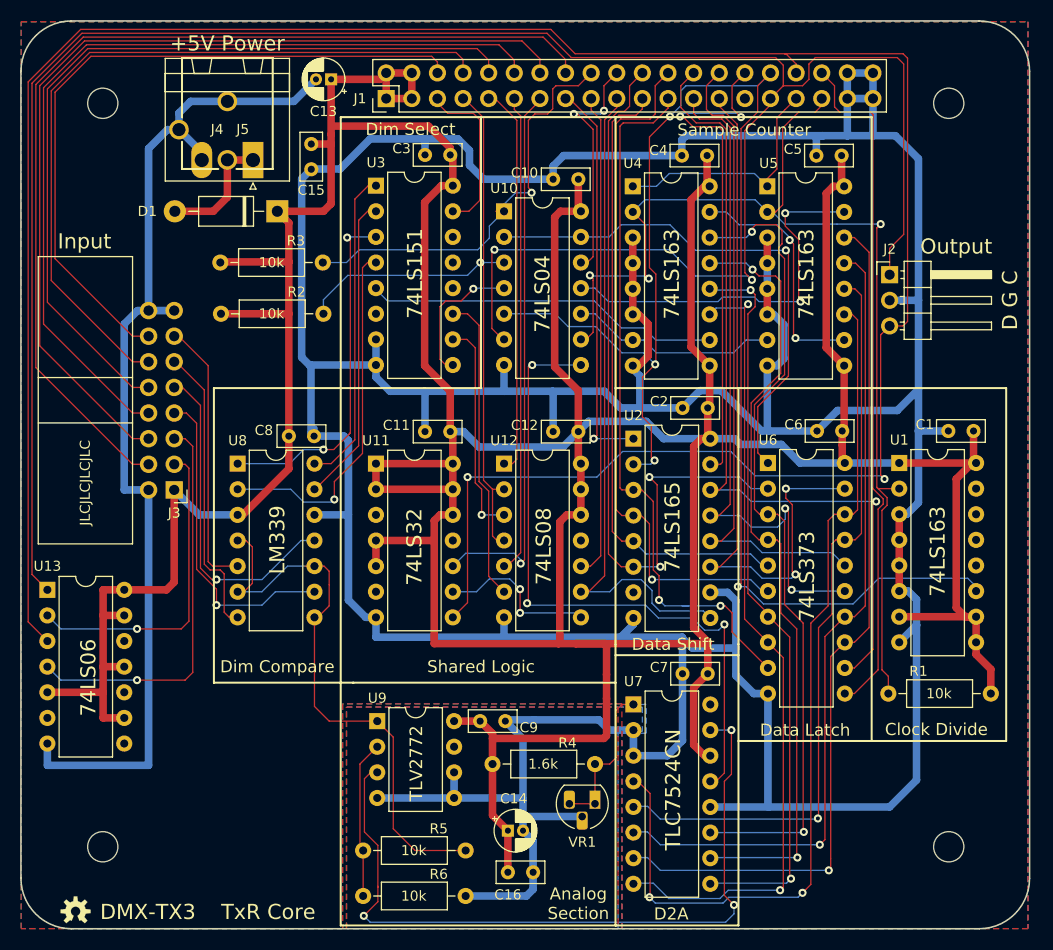
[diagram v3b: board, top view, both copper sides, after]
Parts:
- C1, C10, C11, C12, C15, C16, C2, C3, C4, C5, C6, C7, C8, C9: value .01uF -> 0.1uF
- U13: value ULN2003A -> 74LS06; footprint Package_DIP:DIP-16_W7.62mm -> Package_DIP:DIP-14_W7.62mm
- moved U13 5.24 mm to (89.7, 105.1)
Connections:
- U13 pad 11: Net-(U13-Pad11) -> +5V
- U13 pad 13: Net-(U13-Pad13) -> +5V
- U13 pad 14: Net-(U13-Pad14) -> +5V
- U13 pad 2: /DATA_RX -> /~CLOCK
- U13 pad 3: GND -> /DATA_RX
- U13 pad 4: GND -> /~DATA
- U13 pad 5: GND -> +5V
- U13 pad 6: GND -> Net-(U13-Pad6)
- U13 pad 8: GND -> Net-(U13-Pad8)
- U13 pad 9: Net-(U13-Pad9) -> +5V
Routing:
- net +5V: track 492.7 -> 533.7 mm
- net /~DATA: track 18.7 -> 39.9 mm, vias 0 -> 1
- net /~CLOCK: track 13.3 -> 31.7 mm, vias 0 -> 1
- net GND: track 600.2 -> 611.5 mm
- net /DATA_RX: track 249.0 -> 251.8 mm
- net /~CLK_SLO: track 74.4 -> 76.6 mm
- net /SPD_MID: track 91.7 -> 94.0 mm
- net /~CLK_STEP: track 80.3 -> 82.5 mm
- net /~CLK_FST: track 68.1 -> 70.3 mm
- net /SPD_LO: track 86.3 -> 88.5 mm
- net /SPD_HI: track 97.7 -> 99.9 mm
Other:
- board text added: "74LS04"
- board text added: "74LS06"
- board text added: "74LS08"
- board text added: "74LS151"
- board text added: "74LS163"
- board text added: "74LS165"
- board text added: "74LS32"
- board text added: "74LS373"
- board text added: "DMX-TX3, Rev 1.1 Crazy Giraffe Software"
- board text added: "JLCJLCJLCJLC"
- board text added: "LM339"
- board text added: "TLC7524CN"
- board text added: "TLV2772"
- board text removed: "DMX-TX3, Rev 1.0 Crazy Giraffe Software"
